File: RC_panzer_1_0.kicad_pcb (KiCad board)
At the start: 2 copper layers, 12 parts, among them J1 Conn_01x19_Socket, J10 StepDown_OUT, J2 Conn_01x19_Socket, J3 Motortreiber_links, J4 Motortreiber_rechts, J5 Stepper_driver_links, J6 Stepper_driver_rechts, J7 Screw_Terminal_01x02, J8 Stepper_Ausgang, J9 StepDown_IN

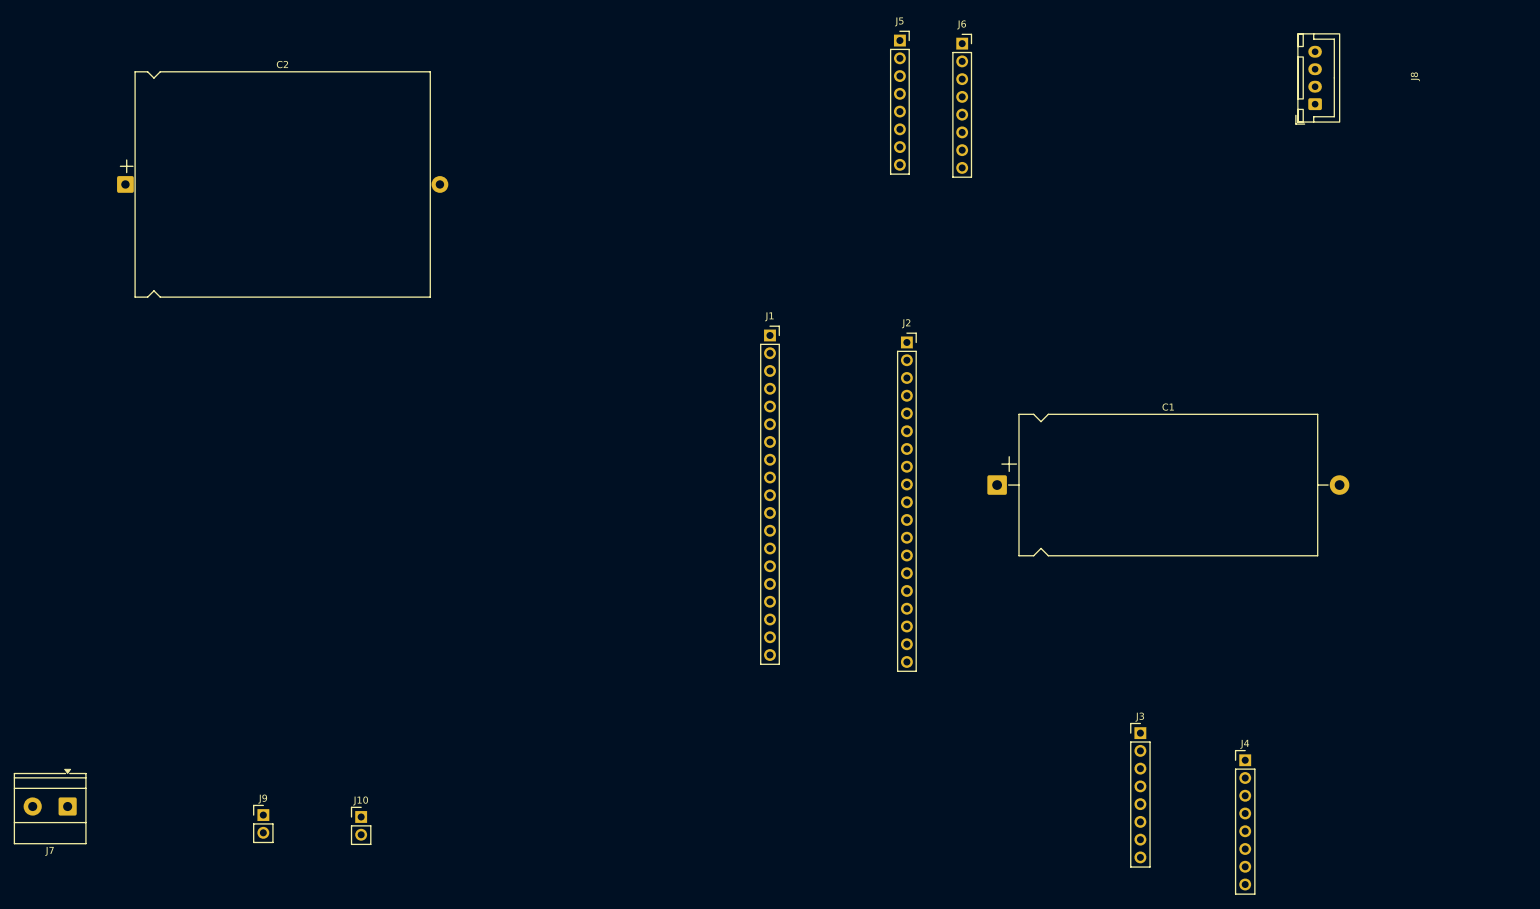
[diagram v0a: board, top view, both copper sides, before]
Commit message: working on h-brige that it continues
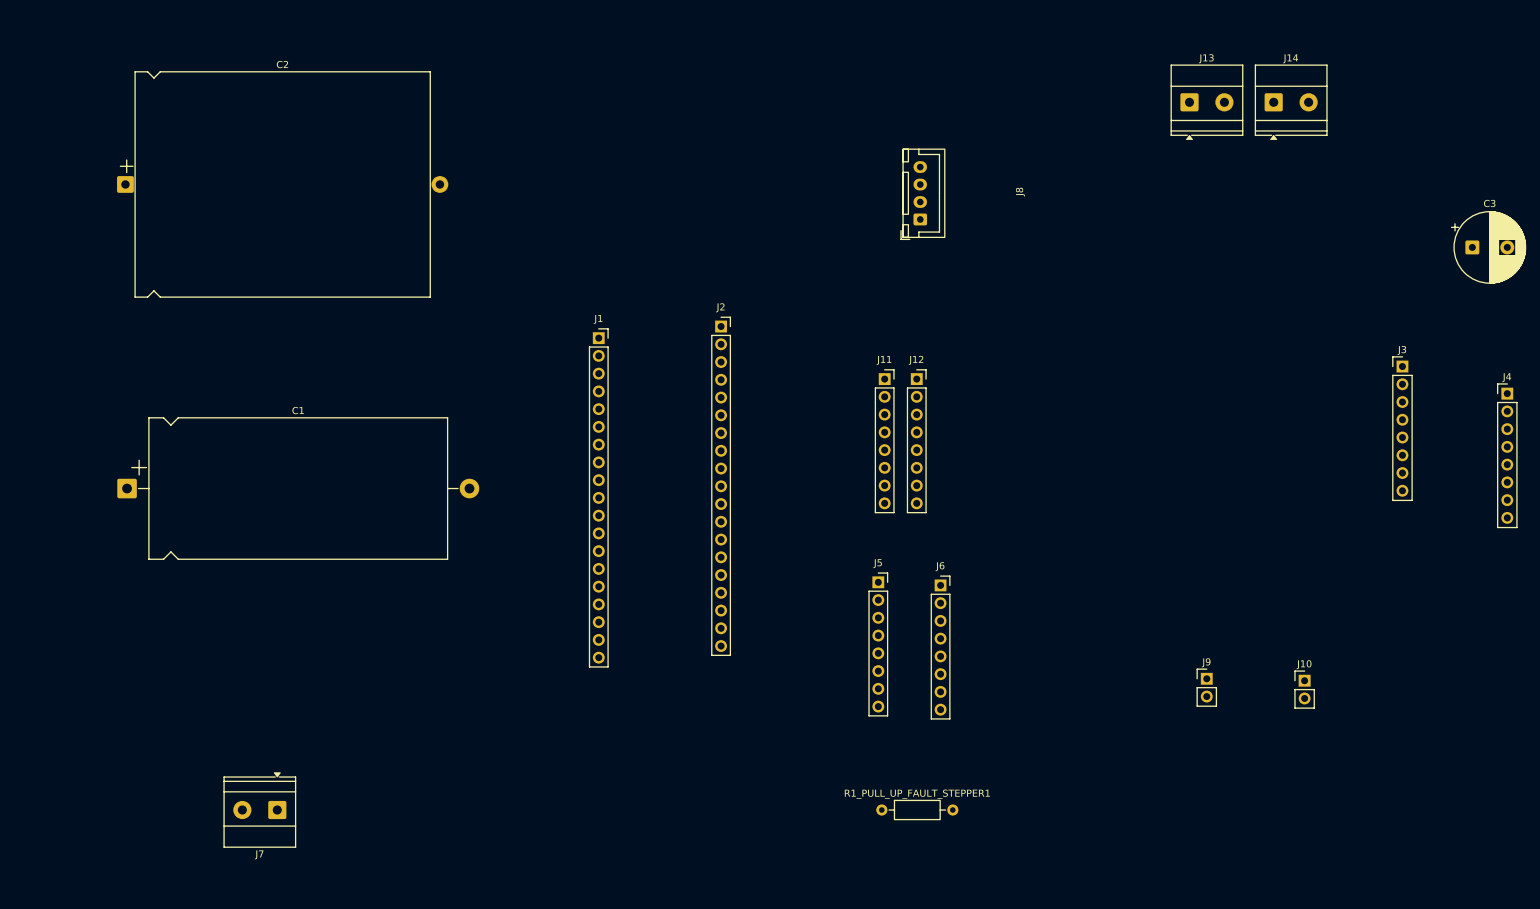
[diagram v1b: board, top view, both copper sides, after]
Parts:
- added C3: 470 uF, Capacitor_THT:CP_Radial_D10.0mm_P5.00mm, F.Cu at (239.5, 58.0)
- added J11: J_TB6612_Links, Connector_PinSocket_2.54mm:PinSocket_1x08_P2.54mm_Vertical, F.Cu at (155.4, 76.8)
- added J12: J_TB6612_Rechts, Connector_PinSocket_2.54mm:PinSocket_1x08_P2.54mm_Vertical, F.Cu at (160.0, 76.8)
- added J13: Screw_Terminal_01x02, TerminalBlock_Phoenix:TerminalBlock_Phoenix_MKDS-1,5-2_1x02_P5.00mm_Horizontal, F.Cu at (199.0, 37.2)
- added J14: Screw_Terminal_01x02, TerminalBlock_Phoenix:TerminalBlock_Phoenix_MKDS-1,5-2_1x02_P5.00mm_Horizontal, F.Cu at (211.1, 37.2)
- added R1_PULL_UP_FAULT_STEPPER1: 10k, Resistor_THT:R_Axial_DIN0207_L6.3mm_D2.5mm_P10.16mm_Horizontal, F.Cu at (155.0, 138.5)
- moved J10 136.4 mm to (215.5, 120.0)
- moved J9 136.4 mm to (201.5, 119.7)
- moved C1 124.5 mm to (47.0, 92.5)
- moved J5 77.6 mm to (154.5, 105.9)
- moved J6 77.6 mm to (163.4, 106.4)
- moved J3 64.5 mm to (229.5, 75.0)
- moved J4 64.5 mm to (244.5, 78.9)
- moved J8 58.9 mm to (160.5, 54.0)
- moved J7 30.0 mm to (68.5, 138.5)
- moved J2 26.7 mm to (132.0, 69.3)
- moved J1 24.5 mm to (114.5, 71.0)
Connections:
- C2 pad 1: /Quelle+ (12V) -> GND
- J1 pad 12: /P14 (GPIO 14) -> /EN_STEPPER
- J1 pad 5: /P34 (GPIO 34 / Input only) -> /FAULT
- J1 pad 8: /P33 (GPIO 33) -> /DIR_STEPPER
- J2 pad 7: /P4 (GPIO 4) -> /M0
- J2 pad 8: /P16 (GPIO 16) -> /M1
- J2 pad 9: /P17 (GPIO 17) -> /M2
- J5 pad 5: /RST_STEPPER -> +3.3V
- J5 pad 6: /SLP_STEPPER -> +3.3V
- J5 pad 7: /STEP_STEPPER -> /P32 (GPIO 32)
- J6 pad 8: /Quelle+ (12V) -> GND
- J7 pad 2: /Quelle+ (12V) -> GND
- J9 pad 2: /Quelle+ (12V) -> GND

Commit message: clearing somthings
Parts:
- removed J3: Motortreiber_links, Connector_PinHeader_2.54mm:PinHeader_1x08_P2.54mm_Vertical
- removed J4: Motortreiber_rechts, Connector_PinHeader_2.54mm:PinHeader_1x08_P2.54mm_Vertical
- C1: footprint Capacitor_THT:CP_Axial_L42.5mm_D20.0mm_P49.00mm_Horizontal -> Capacitor_THT:CP_Radial_D10.0mm_P3.50mm
- C2: footprint Capacitor_THT:CP_Axial_L42.0mm_D32.0mm_P45.00mm_Horizontal -> Capacitor_THT:CP_Radial_D8.0mm_P5.00mm
- moved J9 154.8 mm to (47.0, 129.0), turned to 180 degrees
- moved J10 151.1 mm to (64.5, 126.0)
- moved C2 116.8 mm to (138.0, 122.0), turned to -90 degrees
- moved C3 111.2 mm to (130.0, 38.5)
- moved J8 64.3 mm to (199.0, 105.5)
- moved C1 57.8 mm to (94.5, 125.5), turned to 90 degrees
- moved J2 45.8 mm to (130.5, 115.1), turned to 180 degrees
- moved J7 43.8 mm to (26.0, 128.0)
- moved J11 40.7 mm to (142.5, 38.3)
- moved R1_PULL_UP_FAULT_STEPPER1 30.6 mm to (183.0, 126.1), turned to 90 degrees
- moved J12 21.3 mm to (155.5, 56.0), turned to 180 degrees
- moved J6 17.2 mm to (163.0, 123.6), turned to 180 degrees
- moved J14 14.7 mm to (204.7, 50.5), turned to 90 degrees
- moved J13 9.00 mm to (205.0, 30.5), turned to 90 degrees
- moved J1 1.48 mm to (114.5, 69.5)
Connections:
- C2 pad 1: GND -> /Quelle+ (12V)
- C2 pad 2: /Quelle- (Masse Quelle) -> GND
- C3 pad 1: GND -> /Quelle+ (12V)
- J6 pad 7: /Quelle- (Masse Quelle) -> GND
- J6 pad 8: GND -> /Quelle+ (12V)
- J7 pad 1: /Quelle- (Masse Quelle) -> GND
- J7 pad 2: GND -> /Quelle+ (12V)
- J9 pad 1: /Quelle- (Masse Quelle) -> GND
- J9 pad 2: GND -> /Quelle+ (12V)
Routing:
- net /Quelle+ (12V): track 0.00 -> 131.0 mm
- net /EN_STEPPER: track 0.00 -> 43.5 mm
- net +3.3V: track 0.00 -> 15.9 mm
- net GND: track 0.00 -> 4.51 mm
- net /VIN+ (5V Ausgang Step-Down-Modul): track 0.00 -> 0.65 mm
- added copper zone on F.Cu, net GND
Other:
- board outline added: 233 x 127.5 mm
